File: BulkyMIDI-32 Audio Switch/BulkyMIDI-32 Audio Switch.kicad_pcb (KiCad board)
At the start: 2 copper layers, 100 x 100 mm, 46 parts, among them IC1 0.91_I2C_OLED, J1 DC IN, J10 MIDI IN (ALT), J11 MIDI OUT (ALT), J2 MIDI OUT, J3 MIDI IN, J4 Conn_Power, J5 MIDI THRU, J6 Play_Panel, M1 Mounting, M2 Mounting, M3 Mounting, M4 Mounting, SW1 PLAY, SW2 STOP, SW3 PREV, SW4 NEXT, U1 74HCT14, U2 6N138, U3 6N138

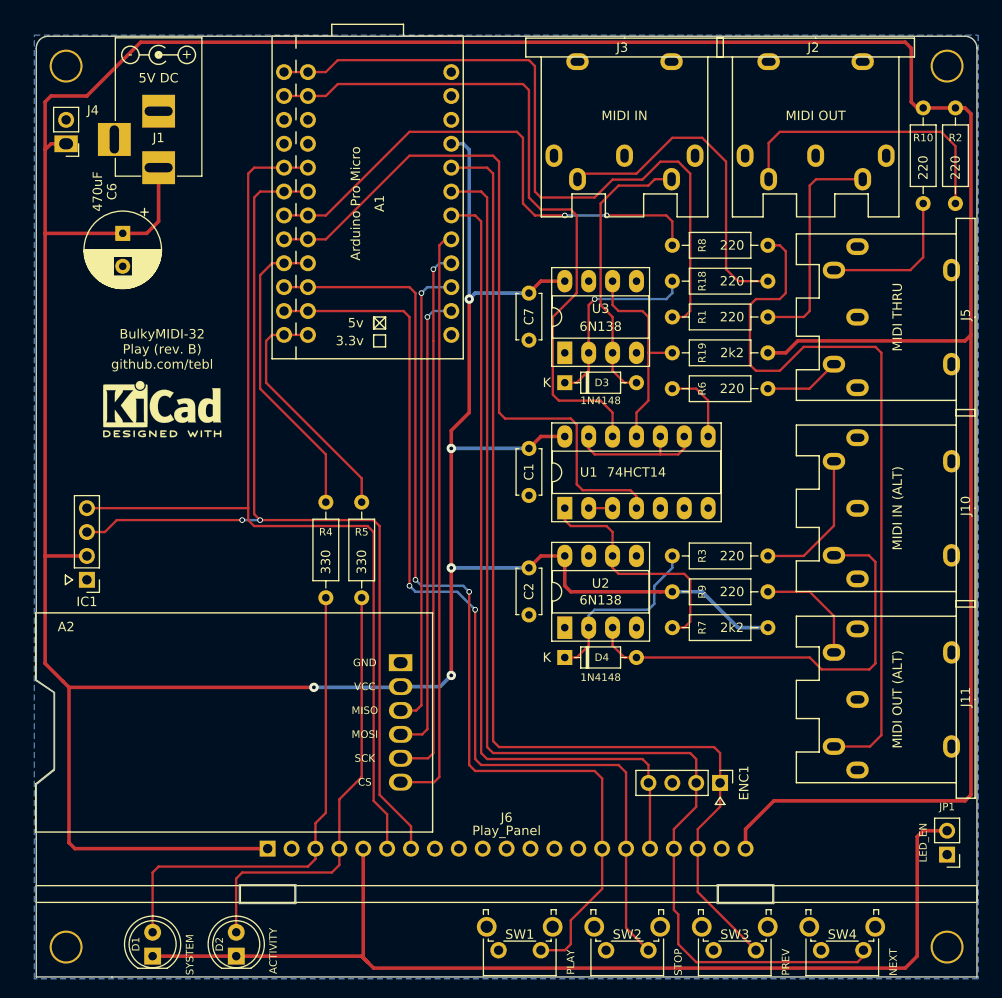
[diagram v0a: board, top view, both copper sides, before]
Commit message: Untested audio switch module
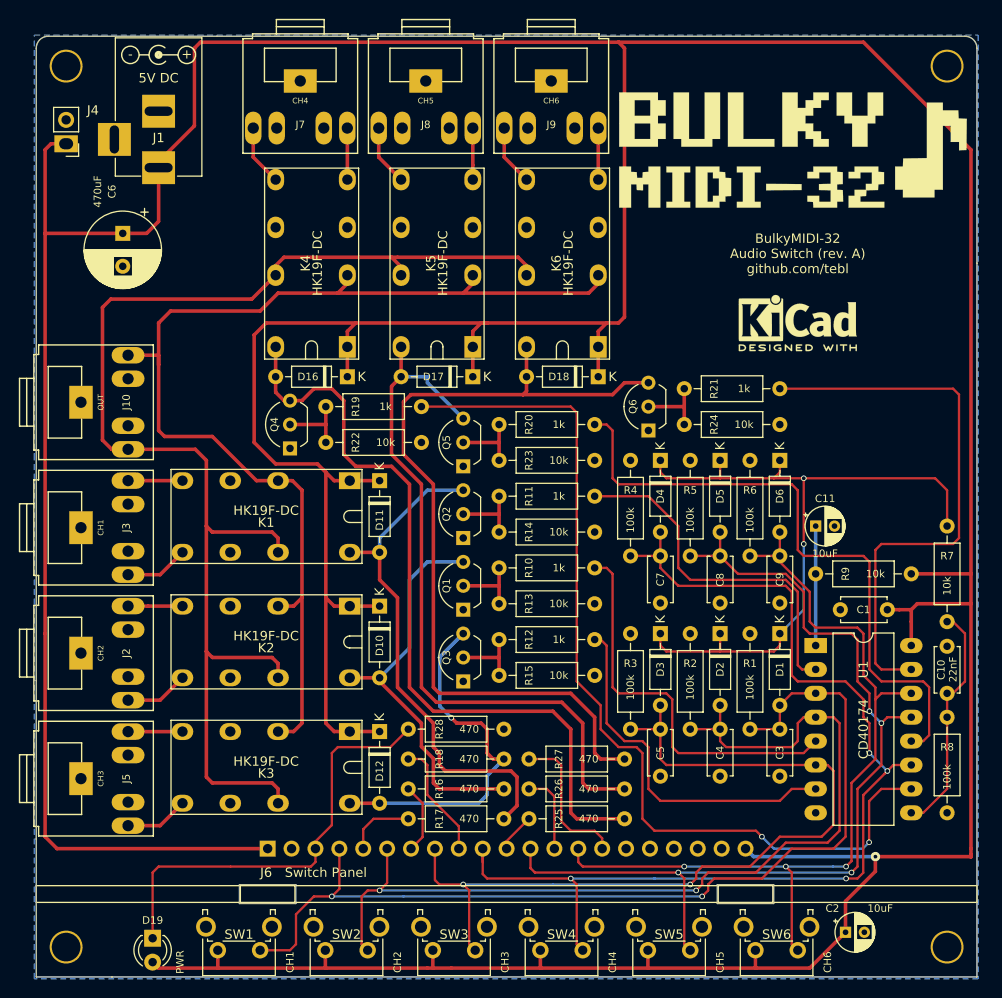
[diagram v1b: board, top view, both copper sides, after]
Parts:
- removed A1: Arduino Pro Micro, arduino_pro_micro:Arduino_Pro_Micro
- removed A2: SD, sd_card_adapter:MicroSD_Card_Adapter
- removed ENC1: Rotary Encoder, Connector_PinHeader_2.54mm:PinHeader_1x04_P2.54mm_Vertical
- removed IC1: 0.91_I2C_OLED, Connector_PinHeader_2.54mm:PinHeader_1x04_P2.54mm_Vertical
- removed J11: MIDI OUT (ALT), BulkyMIDI-32:DIN5_MIDI
- removed JP1: LED_EN, Connector_PinHeader_2.54mm:PinHeader_1x02_P2.54mm_Vertical
- removed U2, U3: 6N138, Package_DIP:DIP-8_W7.62mm_Socket_LongPads
- added C10: 22nF, Capacitor_THT:C_Disc_D4.7mm_W2.5mm_P5.00mm, F.Cu at (167.0, 124.5)
- added C11: 10uF, Capacitor_THT:CP_Radial_D4.0mm_P2.00mm, F.Cu at (153.0, 106.7)
- added C3: 100nF, Capacitor_THT:C_Disc_D4.7mm_W2.5mm_P5.00mm, F.Cu at (149.2, 128.3)
- added C4: 100nF, Capacitor_THT:C_Disc_D4.7mm_W2.5mm_P5.00mm, F.Cu at (142.9, 128.3)
- added C5: 100nF, Capacitor_THT:C_Disc_D4.7mm_W2.5mm_P5.00mm, F.Cu at (136.5, 128.3)
- added C8: 100nF, Capacitor_THT:C_Disc_D4.7mm_W2.5mm_P5.00mm, F.Cu at (142.9, 109.9)
- added C9: 100nF, Capacitor_THT:C_Disc_D4.7mm_W2.5mm_P5.00mm, F.Cu at (149.2, 109.9)
- added D10: 1N4148, Diode_THT:D_DO-35_SOD27_P7.62mm_Horizontal, F.Cu at (106.7, 115.2)
- added D11: 1N4148, Diode_THT:D_DO-35_SOD27_P7.62mm_Horizontal, F.Cu at (106.7, 101.9)
- added D12: 1N4148, Diode_THT:D_DO-35_SOD27_P7.62mm_Horizontal, F.Cu at (106.7, 128.5)
- added D16: 1N4148, Diode_THT:D_DO-35_SOD27_P7.62mm_Horizontal, F.Cu at (103.3, 90.8)
- added D17: 1N4148, Diode_THT:D_DO-35_SOD27_P7.62mm_Horizontal, F.Cu at (116.6, 90.8)
- added D18: 1N4148, Diode_THT:D_DO-35_SOD27_P7.62mm_Horizontal, F.Cu at (129.9, 90.8)
- added D19: PWR, LED_THT:LED_D3.0mm, F.Cu at (82.5, 150.5)
- added D5: 1N4148, Diode_THT:D_DO-35_SOD27_P7.62mm_Horizontal, F.Cu at (142.9, 99.7)
- added D6: 1N4148, Diode_THT:D_DO-35_SOD27_P7.62mm_Horizontal, F.Cu at (149.2, 99.7)
- added G***: LOGO, artwork:BulkyMIDI-32_8bit, F.Cu at (151.1, 66.7)
- added J7: CH4, audio_jack:Tayda_3.5mm_stereo_TRS_jack_A-853, F.Cu at (98.2, 61.0)
- added J8: CH5, audio_jack:Tayda_3.5mm_stereo_TRS_jack_A-853, F.Cu at (111.6, 61.0)
- added J9: CH6, audio_jack:Tayda_3.5mm_stereo_TRS_jack_A-853, F.Cu at (124.9, 61.0)
- added K1: HK19F-DC, HK19F-DC:HK19F-DC, F.Cu at (103.5, 101.9)
- added K2: HK19F-DC, HK19F-DC:HK19F-DC, F.Cu at (103.5, 115.2)
- added K3: HK19F-DC, HK19F-DC:HK19F-DC, F.Cu at (103.5, 128.5)
- added K4: HK19F-DC, HK19F-DC:HK19F-DC, F.Cu at (103.3, 87.6)
- added K5: HK19F-DC, HK19F-DC:HK19F-DC, F.Cu at (116.6, 87.6)
- added K6: HK19F-DC, HK19F-DC:HK19F-DC, F.Cu at (129.9, 87.6)
- added Q1: 2N3904, Package_TO_SOT_THT:TO-92_Inline_Wide, F.Cu at (115.6, 115.6)
- added Q2: 2N3904, Package_TO_SOT_THT:TO-92_Inline_Wide, F.Cu at (115.6, 108.0)
- added Q3: 2N3904, Package_TO_SOT_THT:TO-92_Inline_Wide, F.Cu at (115.6, 123.2)
- added Q4: 2N3904, Package_TO_SOT_THT:TO-92_Inline_Wide, F.Cu at (97.2, 98.4)
- added Q5: 2N3904, Package_TO_SOT_THT:TO-92_Inline_Wide, F.Cu at (115.6, 100.3)
- added Q6: 2N3904, Package_TO_SOT_THT:TO-92_Inline_Wide, F.Cu at (135.3, 96.5)
- added R11: 1k, resistor:R_Axial_DIN0207_L6.3mm_D2.5mm_P10.16mm_Horizontal, F.Cu at (119.4, 103.5)
- added R12: 1k, resistor:R_Axial_DIN0207_L6.3mm_D2.5mm_P10.16mm_Horizontal, F.Cu at (119.4, 118.7)
- added R13: 10k, resistor:R_Axial_DIN0207_L6.3mm_D2.5mm_P10.16mm_Horizontal, F.Cu at (129.5, 114.9)
- added R14: 10k, resistor:R_Axial_DIN0207_L6.3mm_D2.5mm_P10.16mm_Horizontal, F.Cu at (129.5, 107.3)
- added R15: 10k, resistor:R_Axial_DIN0207_L6.3mm_D2.5mm_P10.16mm_Horizontal, F.Cu at (129.5, 122.6)
- added R16: 470, resistor:R_Axial_DIN0207_L6.3mm_D2.5mm_P10.16mm_Horizontal, F.Cu at (119.9, 134.6)
- added R17: 470, resistor:R_Axial_DIN0207_L6.3mm_D2.5mm_P10.16mm_Horizontal, F.Cu at (119.9, 137.8)
- added R20: 1k, resistor:R_Axial_DIN0207_L6.3mm_D2.5mm_P10.16mm_Horizontal, F.Cu at (119.4, 95.9)
- added R21: 1k, resistor:R_Axial_DIN0207_L6.3mm_D2.5mm_P10.16mm_Horizontal, F.Cu at (139.1, 92.1)
- added R22: 10k, resistor:R_Axial_DIN0207_L6.3mm_D2.5mm_P10.16mm_Horizontal, F.Cu at (111.1, 97.8)
- added R23: 10k, resistor:R_Axial_DIN0207_L6.3mm_D2.5mm_P10.16mm_Horizontal, F.Cu at (129.5, 99.7)
- added R24: 10k, resistor:R_Axial_DIN0207_L6.3mm_D2.5mm_P10.16mm_Horizontal, F.Cu at (149.2, 95.9)
- added R25: 470, resistor:R_Axial_DIN0207_L6.3mm_D2.5mm_P10.16mm_Horizontal, F.Cu at (132.7, 137.8)
- added R26: 470, resistor:R_Axial_DIN0207_L6.3mm_D2.5mm_P10.16mm_Horizontal, F.Cu at (132.7, 134.6)
- added R27: 470, resistor:R_Axial_DIN0207_L6.3mm_D2.5mm_P10.16mm_Horizontal, F.Cu at (132.7, 131.4)
- added R28: 470, resistor:R_Axial_DIN0207_L6.3mm_D2.5mm_P10.16mm_Horizontal, F.Cu at (119.9, 128.3)
- added SW5: CH5, Button_Switch_THT:SW_Tactile_SPST_Angled_PTS645Vx39-2LFS, F.Cu at (139.7, 151.8)
- added SW6: CH6, Button_Switch_THT:SW_Tactile_SPST_Angled_PTS645Vx39-2LFS, F.Cu at (151.1, 151.8)
- C2: value 100nF -> 10uF; footprint Capacitor_THT:C_Disc_D4.7mm_W2.5mm_P5.00mm -> Capacitor_THT:CP_Radial_D4.0mm_P2.00mm
- D1: value SYSTEM -> 1N4148; footprint LED_THT:LED_D5.0mm -> Diode_THT:D_DO-35_SOD27_P7.62mm_Horizontal
- D2: value ACTIVITY -> 1N4148; footprint LED_THT:LED_D5.0mm -> Diode_THT:D_DO-35_SOD27_P7.62mm_Horizontal
- J10: value MIDI IN (ALT) -> OUT; footprint BulkyMIDI-32:DIN5_MIDI -> audio_jack:Tayda_3.5mm_stereo_TRS_jack_A-853
- J2: value MIDI OUT -> CH2; footprint BulkyMIDI-32:DIN5_MIDI -> audio_jack:Tayda_3.5mm_stereo_TRS_jack_A-853
- J3: value MIDI IN -> CH1; footprint BulkyMIDI-32:DIN5_MIDI -> audio_jack:Tayda_3.5mm_stereo_TRS_jack_A-853
- J5: value MIDI THRU -> CH3; footprint BulkyMIDI-32:DIN5_MIDI -> audio_jack:Tayda_3.5mm_stereo_TRS_jack_A-853
- J6: value Play_Panel -> Switch Panel; footprint BulkyMIDI-32:Play_Panel -> BulkyMIDI-32:Switch_Panel
- R1, R2, R3, R6, R8: value 220 -> 100k
- R10: value 220 -> 1k
- R18: value 220 -> 470
- R19: value 2k2 -> 1k
- R4, R5: value 330 -> 100k
- R7: value 2k2 -> 10k
- R9: value 220 -> 10k
- SW1: value PLAY -> CH1
- SW2: value STOP -> CH2
- SW3: value PREV -> CH3
- SW4: value NEXT -> CH4
- U1: value 74HCT14 -> CD40174; footprint Package_DIP:DIP-14_W7.62mm_Socket_LongPads -> Package_DIP:DIP-16_W10.16mm_LongPads
- moved J5 94.7 mm to (76.5, 133.5)
- moved J2 93.0 mm to (76.5, 120.2), turned to 90 degrees
- moved J10 81.7 mm to (76.5, 93.5)
- moved D1 75.0 mm to (149.2, 118.1), turned to 270 degrees
- moved R2 71.8 mm to (139.7, 128.3), turned to 90 degrees
- moved J3 68.7 mm to (76.5, 106.8), turned to 90 degrees
- moved REF*** 68.2 mm to (151.1, 85.1)
- moved R10 66.5 mm to (119.4, 111.1), turned to 0 degrees
- moved D2 61.8 mm to (142.9, 118.1), turned to 270 degrees
- moved R18 53.9 mm to (119.9, 131.4), turned to 180 degrees
- moved R8 53.7 mm to (167.0, 127.0), turned to 270 degrees
- moved C2 51.3 mm to (156.2, 149.9), turned to 0 degrees
- moved R19 47.3 mm to (101.0, 94.0), turned to 0 degrees
- moved R1 43.9 mm to (146.1, 128.3), turned to 90 degrees
- moved C1 41.8 mm to (160.7, 115.6), turned to 180 degrees
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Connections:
- C7 pad 1: +5V -> /SW4
- D1 pad 1: /COM -> Net-(D1-Pad1)
- D1 pad 2: /SYS -> /SW1
- D2 pad 1: /COM -> Net-(D1-Pad1)
- D2 pad 2: /ACT -> /SW2
- D3 pad 1: Net-(D3-Pad1) -> Net-(D1-Pad1)
- D3 pad 2: Net-(D3-Pad2) -> /SW3
- D4 pad 1: Net-(D4-Pad1) -> Net-(D1-Pad1)
- D4 pad 2: Net-(D4-Pad2) -> /SW4
- J10 pad 1: (no net) -> GND
- J10 pad 2: (no net) -> /RIGHT
- J10 pad 4: Net-(J10-Pad4) -> (no net)
- J10 pad 5: Net-(D4-Pad2) -> /LEFT
- J2 pad 1: (no net) -> GND
- J2 pad 2: GND -> Net-(J2-Pad2)
- J2 pad 4: Net-(J2-Pad4) -> (no net)
- J3 pad 1: (no net) -> GND
- J3 pad 2: (no net) -> Net-(J3-Pad2)
- J3 pad 4: Net-(J3-Pad4) -> (no net)
- J3 pad 5: Net-(D3-Pad2) -> Net-(J3-Pad5)
- J5 pad 1: (no net) -> GND
- J5 pad 2: GND -> Net-(J5-Pad2)
- J5 pad 4: Net-(J5-Pad4) -> (no net)
- J6 pad 10: (no net) -> /SW4
- J6 pad 11: (no net) -> /LED4
- J6 pad 12: (no net) -> /SW5
- J6 pad 13: (no net) -> /LED5
- J6 pad 14: (no net) -> /SW6
- J6 pad 15: /PLAY -> /LED6
- J6 pad 16: /STOP -> (no net)
- J6 pad 17: /RE_BTN -> (no net)
- J6 pad 18: /RE_CLK -> (no net)
- J6 pad 19: /RE_DAT -> (no net)
- J6 pad 3: /SYS -> /PWR
- J6 pad 4: /ACT -> /SW1
- J6 pad 5: /COM -> /LED1
- J6 pad 6: /SDA -> /SW2
- J6 pad 7: /SCL -> /LED2
- J6 pad 8: (no net) -> /SW3
- J6 pad 9: (no net) -> /LED3
- R1 pad 1: Net-(J2-Pad5) -> /SW1
- R1 pad 2: MIDI_OUT -> GND
- R10 pad 1: +5V -> Net-(Q1-Pad2)
- R10 pad 2: Net-(J5-Pad4) -> /CH2
- R18 pad 1: Net-(D3-Pad1) -> Net-(D12-Pad2)
- R18 pad 2: Net-(J3-Pad4) -> /LED3
- R19 pad 1: +5V -> Net-(Q4-Pad2)
- R19 pad 2: Net-(R19-Pad2) -> /CH4
- R2 pad 1: +5V -> /SW2
- R2 pad 2: Net-(J2-Pad4) -> GND
- R3 pad 1: Net-(D4-Pad1) -> /SW3
- R3 pad 2: Net-(J10-Pad4) -> GND
- R4 pad 1: Net-(A1-Pad9) -> /SW4
- R4 pad 2: /SYS -> GND
- R5 pad 1: Net-(A1-Pad12) -> /SW5
- R5 pad 2: /ACT -> GND
- R6 pad 1: Net-(J5-Pad5) -> /SW6
- R6 pad 2: MIDI_THRU -> GND
- R7 pad 1: +5V -> Net-(C10-Pad1)
- R7 pad 2: Net-(R7-Pad2) -> Net-(D1-Pad1)
- R8 pad 1: Net-(J11-Pad5) -> Net-(C10-Pad1)
- R8 pad 2: MIDI_OUT2 -> GND
- R9 pad 2: Net-(J11-Pad4) -> Net-(C11-Pad1)
- SW1 pad 1: /PLAY -> /SW1
- SW1 pad 2: GND -> +5V
- SW2 pad 1: /STOP -> /SW2
- SW2 pad 2: GND -> +5V
- SW3 pad 1: /RE_DAT -> /SW3
- SW3 pad 2: GND -> +5V
- SW4 pad 1: /RE_CLK -> /SW4
- SW4 pad 2: GND -> +5V
- U1 pad 1: Net-(R7-Pad2) -> Net-(C11-Pad1)
- U1 pad 10: Net-(U1-Pad10) -> /CH4
- U1 pad 11: Net-(R19-Pad2) -> /SW4
- U1 pad 12: MIDI_IN -> /CH5
- U1 pad 13: Net-(U1-Pad10) -> /SW5
- U1 pad 14: +5V -> /SW6
- U1 pad 2: Net-(U1-Pad2) -> /CH1
- U1 pad 3: Net-(U1-Pad2) -> /SW1
- U1 pad 4: MIDI_IN2 -> /SW2
- U1 pad 5: GND -> /CH2
- U1 pad 6: (no net) -> /SW3
- U1 pad 7: GND -> /CH3
- U1 pad 8: MIDI_THRU -> GND
- U1 pad 9: Net-(U1-Pad10) -> Net-(C10-Pad1)
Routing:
- net /LEFT: track 0.00 -> 140.3 mm
- net /RE_CLK: track 127.5 -> 0.00 mm
- net /RIGHT: track 0.00 -> 118.2 mm
- net /SW4: track 0.00 -> 116.1 mm, vias 0 -> 4
- net /RE_DAT: track 114.2 -> 0.00 mm
- net /COM: track 110.7 -> 0.00 mm
- net /SDA: track 108.7 -> 0.00 mm
- net /SCL: track 108.1 -> 0.00 mm, vias 2 -> 0
- net /PLAY: track 106.5 -> 0.00 mm, vias 2 -> 0
- net /SW1: track 0.00 -> 103.0 mm, vias 0 -> 2
- net /STOP: track 102.6 -> 0.00 mm, vias 2 -> 0
- net /SW5: track 0.00 -> 102.0 mm, vias 0 -> 4
- net /CH4: track 0.00 -> 99.0 mm, vias 0 -> 2
- net /SW2: track 0.00 -> 98.9 mm, vias 0 -> 2
- net /SW6: track 0.00 -> 90.4 mm, vias 0 -> 3
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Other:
- outline, holes or cut-outs redrawn
- net class Sound added: clearance 0.2, trace_width 0.381, via_dia 1, via_drill 0.4
- board text added: "BulkyMIDI-32 Audio Switch (rev. A) github.com/tebl"
- board text added: "CH1"
- board text added: "CH2"
- board text added: "CH3"
- board text added: "CH4"
- board text added: "CH5"
- board text added: "CH6"
- board text added: "OUTPUT"
- board text removed: "BulkyMIDI-32 Play (rev. B) github.com/tebl"
- board text removed: "MICRO SD"
- board text removed: "MIDI IN"
- board text removed: "MIDI IN (ALT)"
- board text removed: "MIDI OUT"
- board text removed: "MIDI OUT (ALT)"
- board text removed: "MIDI THRU"

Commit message: Audio Switch FP1
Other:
- board text added: "JLCJLCJLCJLC"

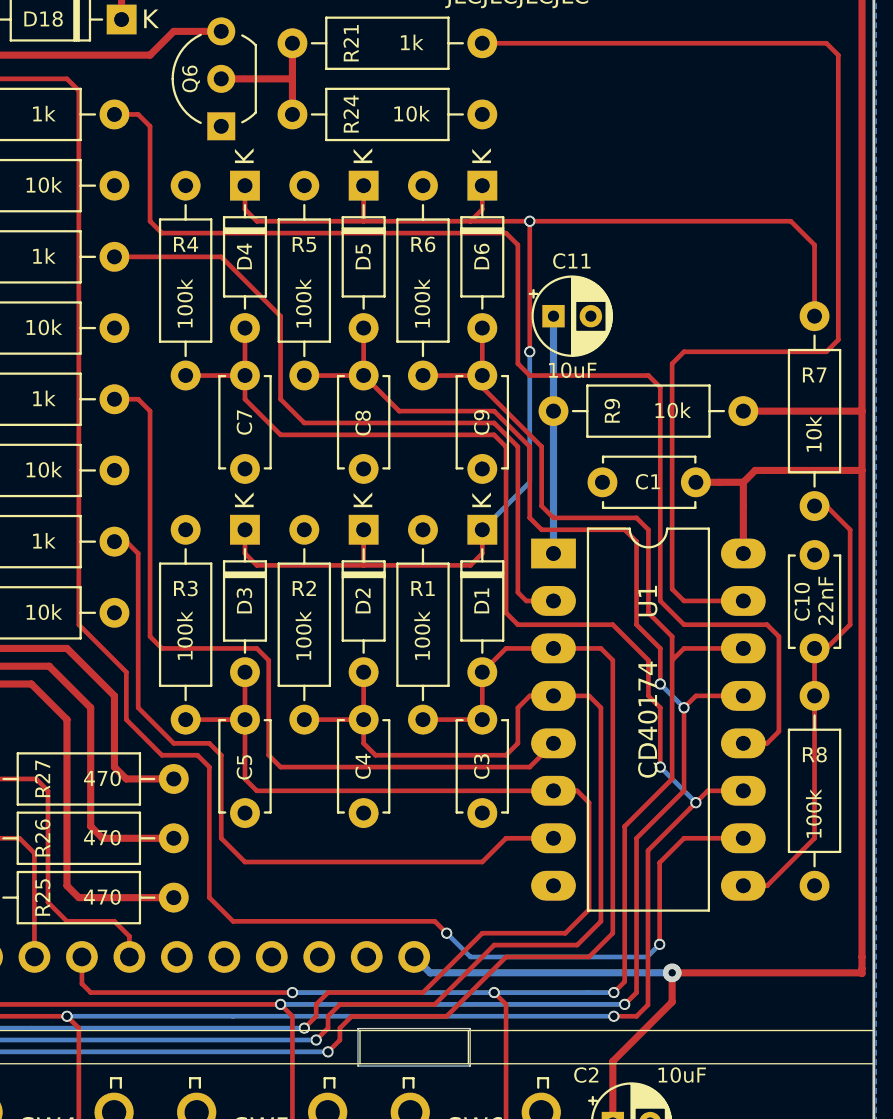
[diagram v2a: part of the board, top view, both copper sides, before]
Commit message: Fix weird socket selection
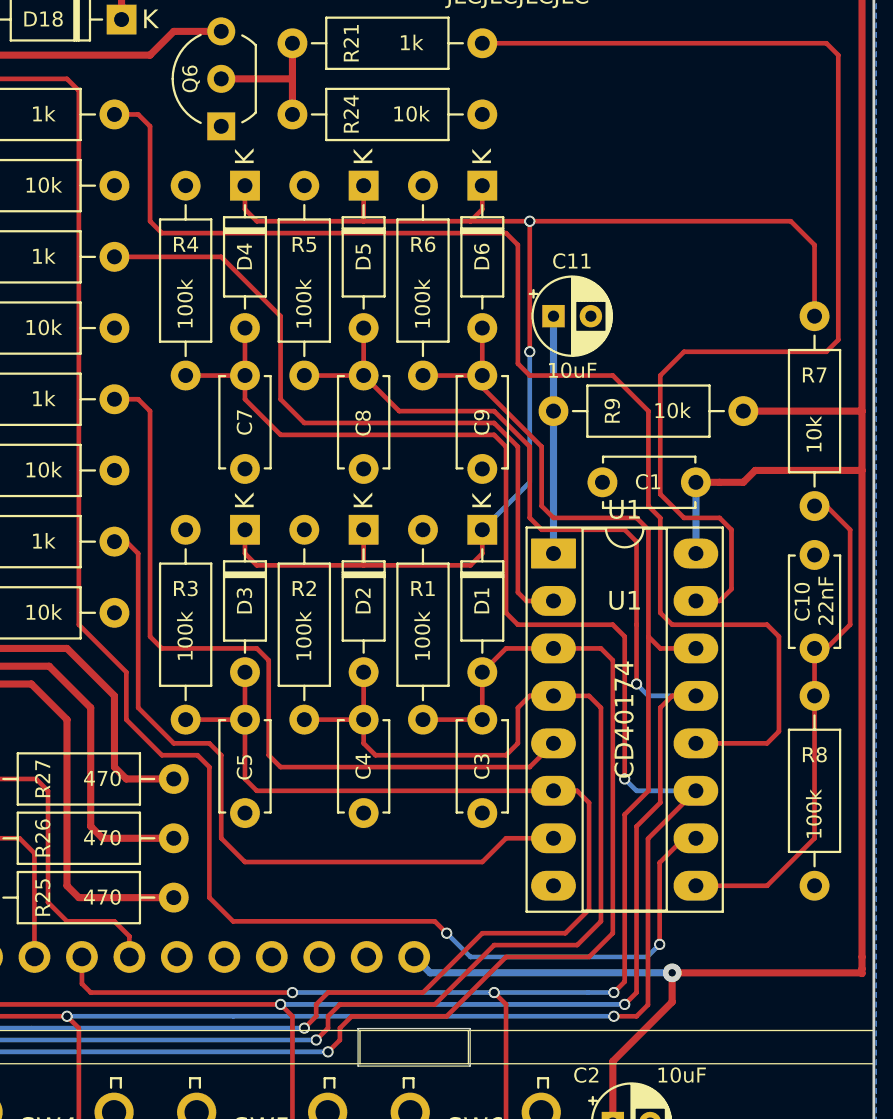
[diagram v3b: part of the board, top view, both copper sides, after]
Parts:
- U1: footprint Package_DIP:DIP-16_W10.16mm_LongPads -> Package_DIP:DIP-16_W7.62mm_Socket_LongPads
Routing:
- net /CH4: track 99.0 -> 95.9 mm
- net Net-(C10-Pad1): track 25.0 -> 27.5 mm
- net /SW6: track 90.4 -> 88.1 mm
- net /CH5: track 67.8 -> 69.6 mm
- net /CH6: track 60.1 -> 61.2 mm
- net /SW4: track 116.1 -> 115.2 mm, vias 4 -> 3
- net /SW5: track 102.0 -> 101.3 mm, vias 4 -> 3

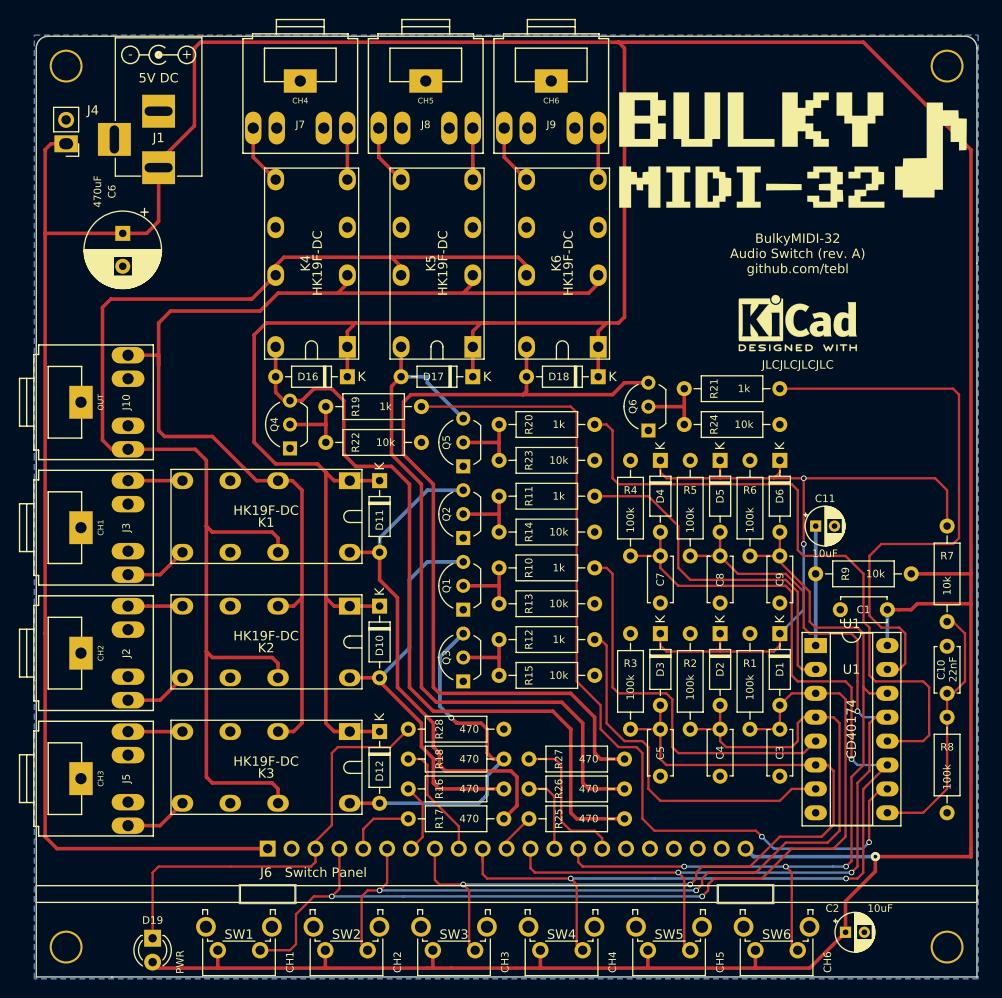
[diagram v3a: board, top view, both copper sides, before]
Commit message: Change R7 value
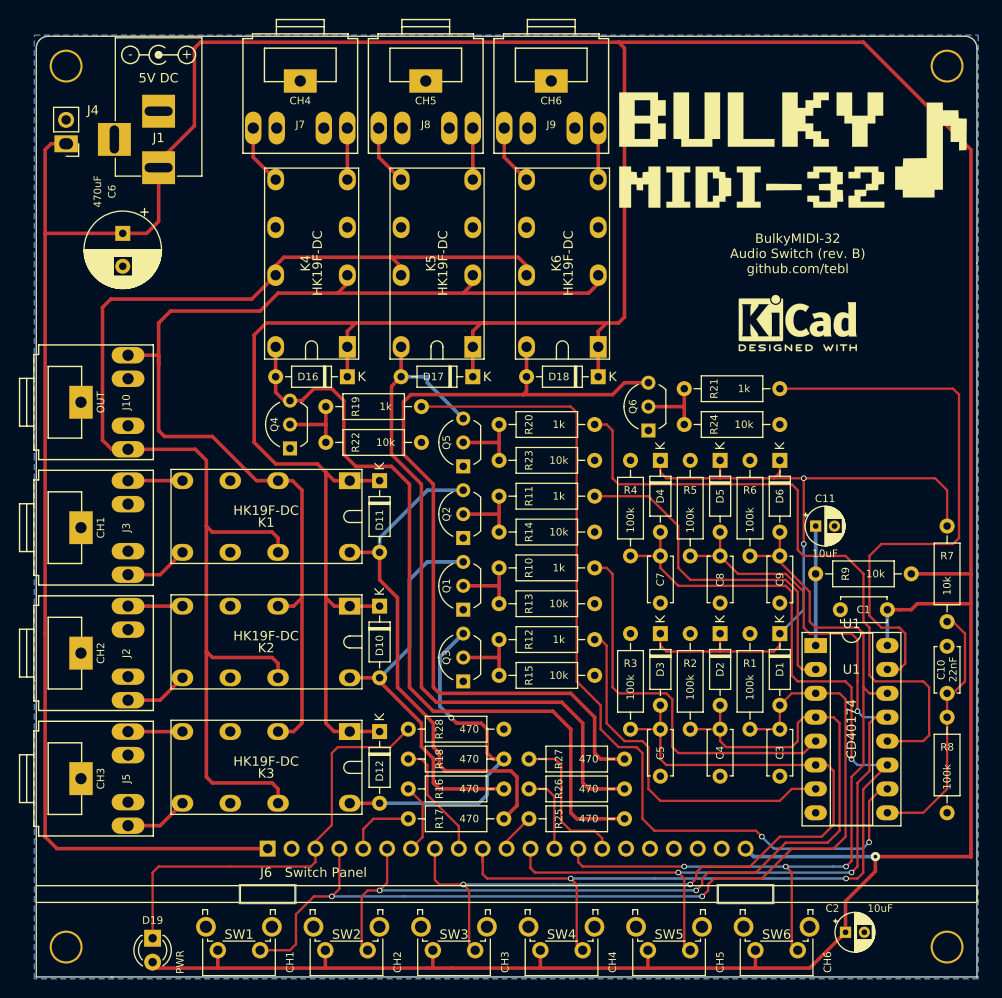
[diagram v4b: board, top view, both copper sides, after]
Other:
- board text added: "BulkyMIDI-32 Audio Switch (rev. B) github.com/tebl"
- board text removed: "BulkyMIDI-32 Audio Switch (rev. A) github.com/tebl"
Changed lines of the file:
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@@
     )
     (fp_text value CH2 (at 0 0.508 90) (layer F.SilkS)
-      (effects (font (size 0.6 0.6) (thickness 0.1)))
+      (effects (font (size 0.8 0.8) (thickness 0.1)))
     )
     (fp_line (start -1.778 -1.524) (end -3.81 -1.524) (layer F.SilkS) (width 0.15))
@@
     )
     (fp_text value CH1 (at 0 0.508 90) (layer F.SilkS)
-      (effects (font (size 0.6 0.6) (thickness 0.1)))
+      (effects (font (size 0.8 0.8) (thickness 0.1)))
     )
     (fp_line (start -1.778 -1.524) (end -3.81 -1.524) (layer F.SilkS) (width 0.15))
@@
     )
     (fp_text value CH3 (at 0 0.508 90) (layer F.SilkS)
-      (effects (font (size 0.6 0.6) (thickness 0.1)))
+      (effects (font (size 0.8 0.8) (thickness 0.1)))
     )
     (fp_line (start -1.778 -1.524) (end -3.81 -1.524) (layer F.SilkS) (width 0.15))
@@
     )
     (fp_text value CH4 (at 0 0.508) (layer F.SilkS)
-      (effects (font (size 0.6 0.6) (thickness 0.1)))
+      (effects (font (size 0.8 0.8) (thickness 0.1)))
     )
     (fp_line (start 6.096 6.096) (end -6.096 6.096) (layer F.SilkS) (width 0.15))
@@
     )
     (fp_text value CH5 (at 0 0.508) (layer F.SilkS)
-      (effects (font (size 0.6 0.6) (thickness 0.1)))
+      (effects (font (size 0.8 0.8) (thickness 0.1)))
     )
     (fp_line (start 6.096 6.096) (end -6.096 6.096) (layer F.SilkS) (width 0.15))
@@
     )
     (fp_text value CH6 (at 0 0.508) (layer F.SilkS)
-      (effects (font (size 0.6 0.6) (thickness 0.1)))
+      (effects (font (size 0.8 0.8) (thickness 0.1)))
     )
     (fp_line (start 6.096 6.096) (end -6.096 6.096) (layer F.SilkS) (width 0.15))
@@
     )
     (fp_text value OUT (at 0 0.508 90) (layer F.SilkS)
-      (effects (font (size 0.6 0.6) (thickness 0.1)))
+      (effects (font (size 0.8 0.8) (thickness 0.1)))
     )
     (fp_line (start 6.096 6.096) (end -6.096 6.096) (layer F.SilkS) (width 0.15))
@@
     )
   )
-  (gr_text JLCJLCJLCJLC (at 151.13 89.535) (layer F.SilkS)
+  (gr_text JLCJLCJLCJLC (at 151.13 89.535) (layer F.Fab)
     (effects (font (size 0.9 0.9) (thickness 0.1)))
   )
@@
     (effects (font (size 0.8 0.8) (thickness 0.1)) (justify mirror))
   )
-  (gr_text "BulkyMIDI-32\nAudio Switch (rev. A)\ngithub.com/tebl" (at 151.13 77.724) (layer F.SilkS)
+  (gr_text "BulkyMIDI-32\nAudio Switch (rev. B)\ngithub.com/tebl" (at 151.13 77.724) (layer F.SilkS)
     (effects (font (size 1 1) (thickness 0.15)))
   )

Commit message: Add README
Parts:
- moved C2 1.02 mm to (155.2, 149.9)
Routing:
- net +5V: track 588.9 -> 589.7 mm
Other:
- board text removed: "JLCJLCJLCJLC"

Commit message: Added alternate output placement
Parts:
- added J11: OUT_ALT, audio_jack:Tayda_3.5mm_stereo_TRS_jack_A-853, F.Cu at (147.3, 61.0)
- moved REF*** 18.0 mm to (160.7, 100.3)
- moved G*** 12.1 mm to (151.1, 78.7)
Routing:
- net /RIGHT: track 118.2 -> 158.0 mm
- net /LEFT: track 140.3 -> 173.8 mm
- net +5V: track 589.7 -> 575.0 mm
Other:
- board text added: "BulkyMIDI-32 Audio Switch (rev. C) github.com/tebl"
- board text removed: "BulkyMIDI-32 Audio Switch (rev. B) github.com/tebl"
